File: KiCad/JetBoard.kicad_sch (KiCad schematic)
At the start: 11 parts, among them J1 USB_C_Receptacle_USB2.0_16P, J3 Conn_01x04

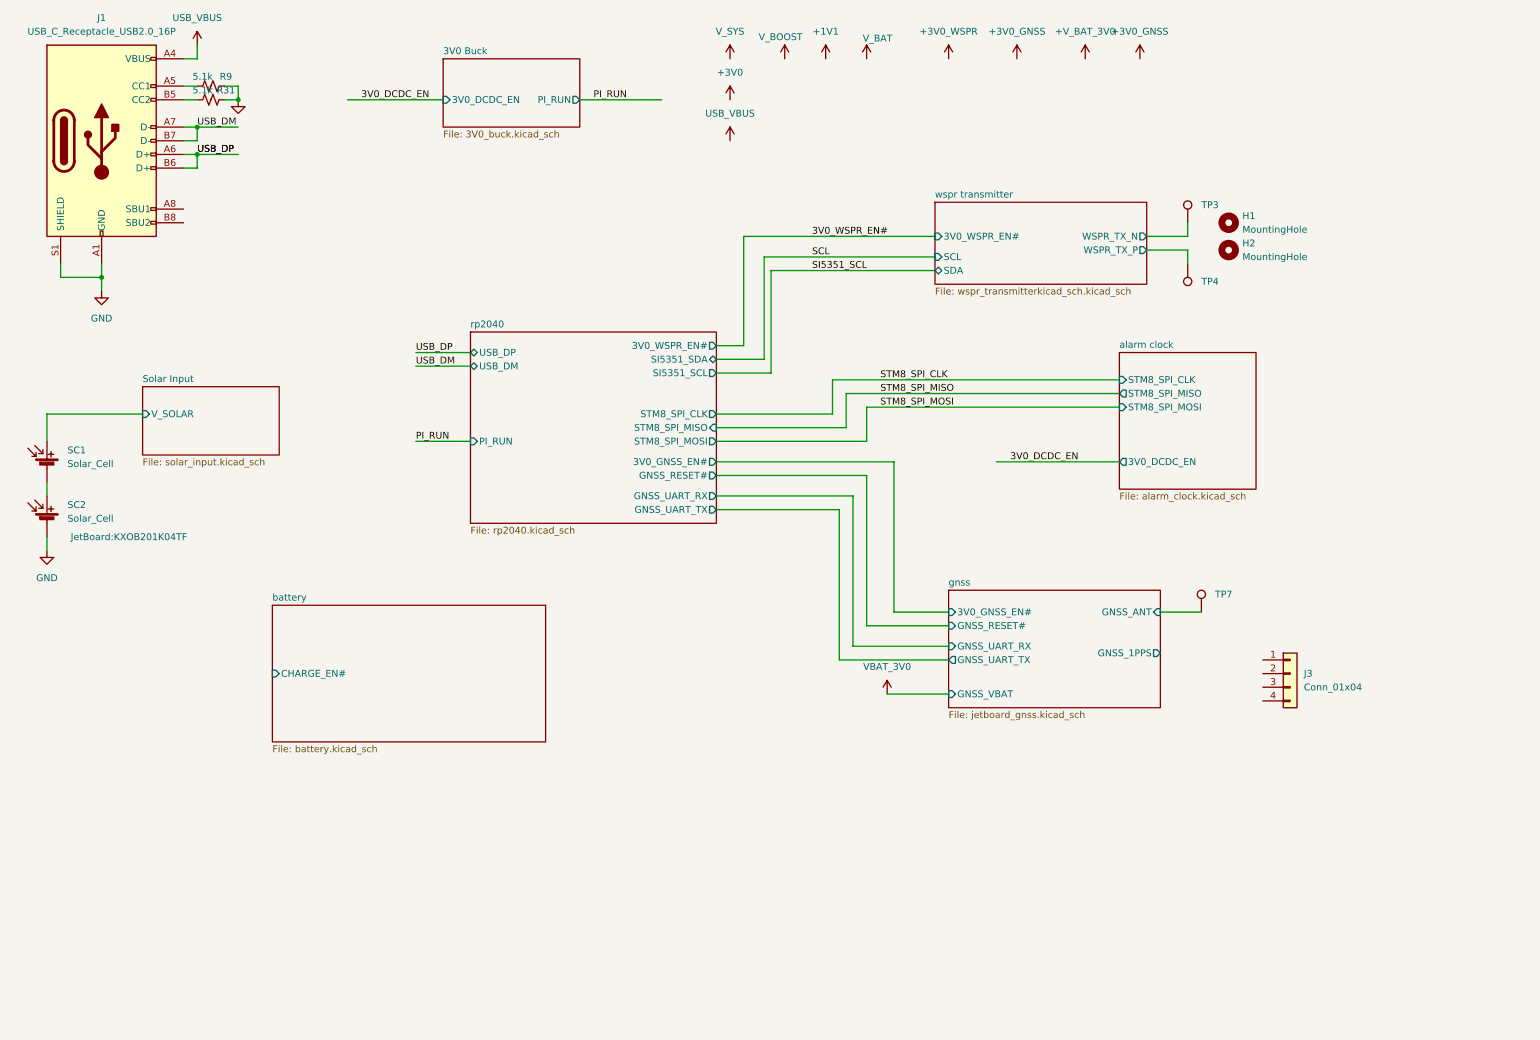
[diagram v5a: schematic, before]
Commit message: Clean up ERC errors
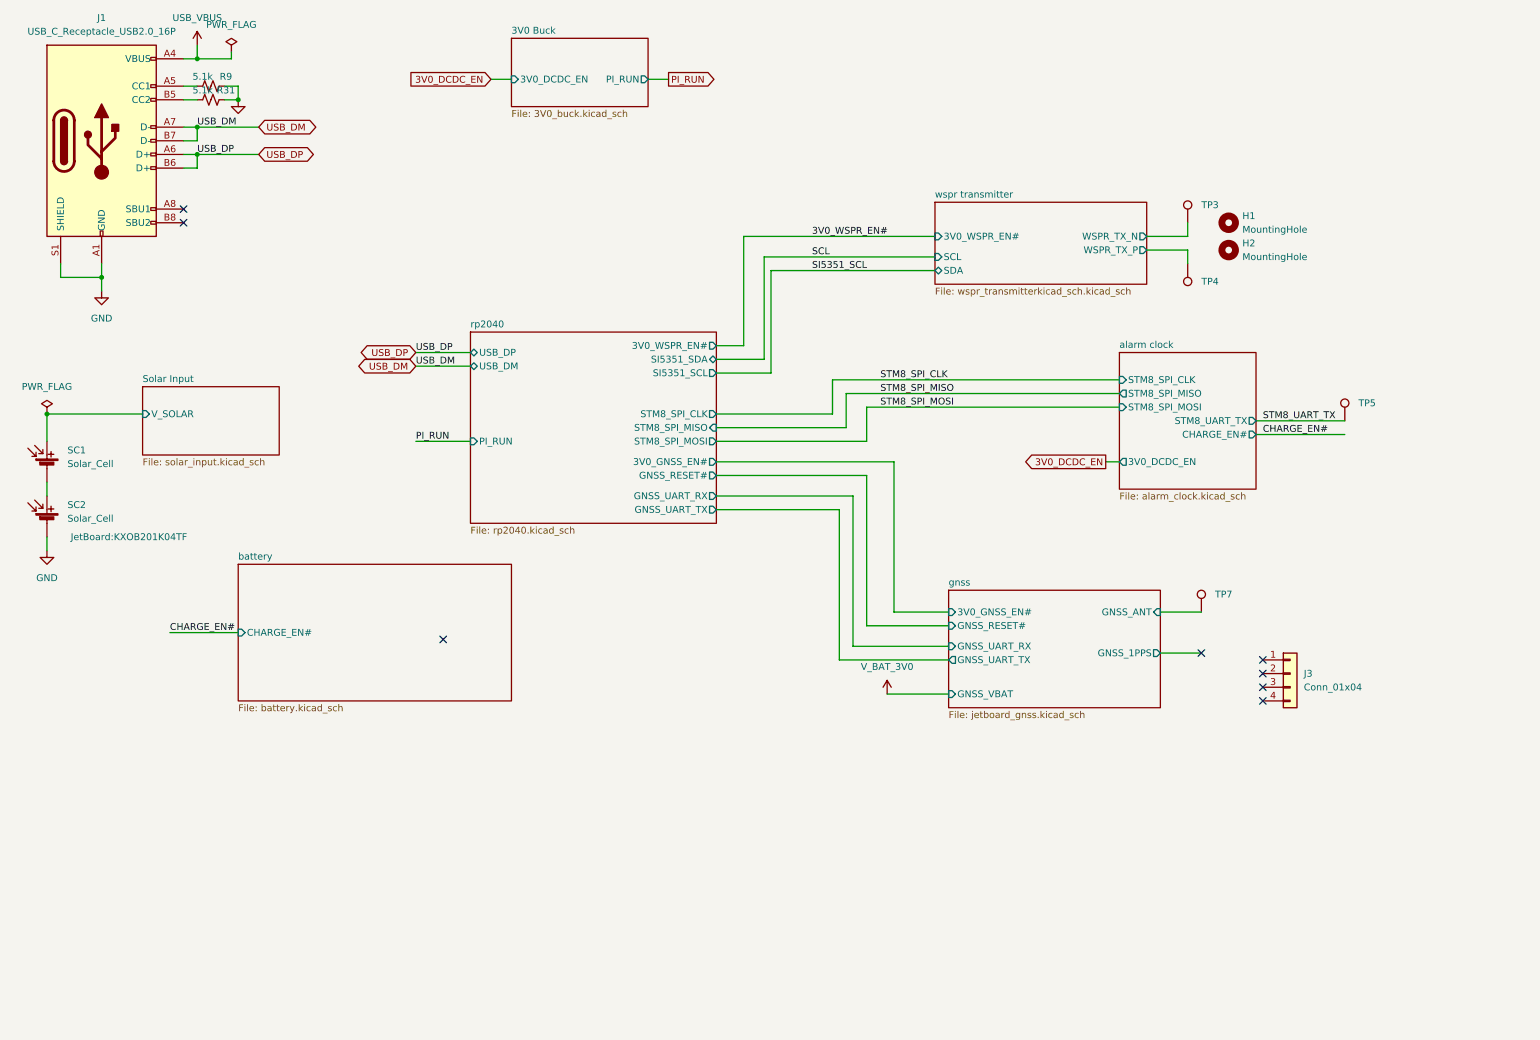
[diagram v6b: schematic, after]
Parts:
- added TP5: TestPoint, TestPoint:TestPoint_Pad_1.5x1.5mm, symbol Connector:TestPoint
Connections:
- new net STM8_UART_TX: TP5.1
- no-connect marks 0 -> 8
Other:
- sheet alarm clock ports: added CHARGE_EN#, STM8_UART_TX; removed none

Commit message: DRC cleanup
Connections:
- no-connect marks 8 -> 7

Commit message: Mods
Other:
- sheet alarm clock ports: added ~{CHARGE_EN}; removed CHARGE_EN#
- sheet battery ports: added ~{CHARGE_EN}; removed CHARGE_EN#
